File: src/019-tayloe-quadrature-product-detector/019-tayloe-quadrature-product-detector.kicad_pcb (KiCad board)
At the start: 2 copper layers, 20 x 65 mm, 30 parts, among them J1 CONN, J2 CONN, J3 CONN, J4 CONN, J5 CONN, J6 CONN, J7 VCC, J8 VA, J9 VE, U1 74LVX74MTCX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

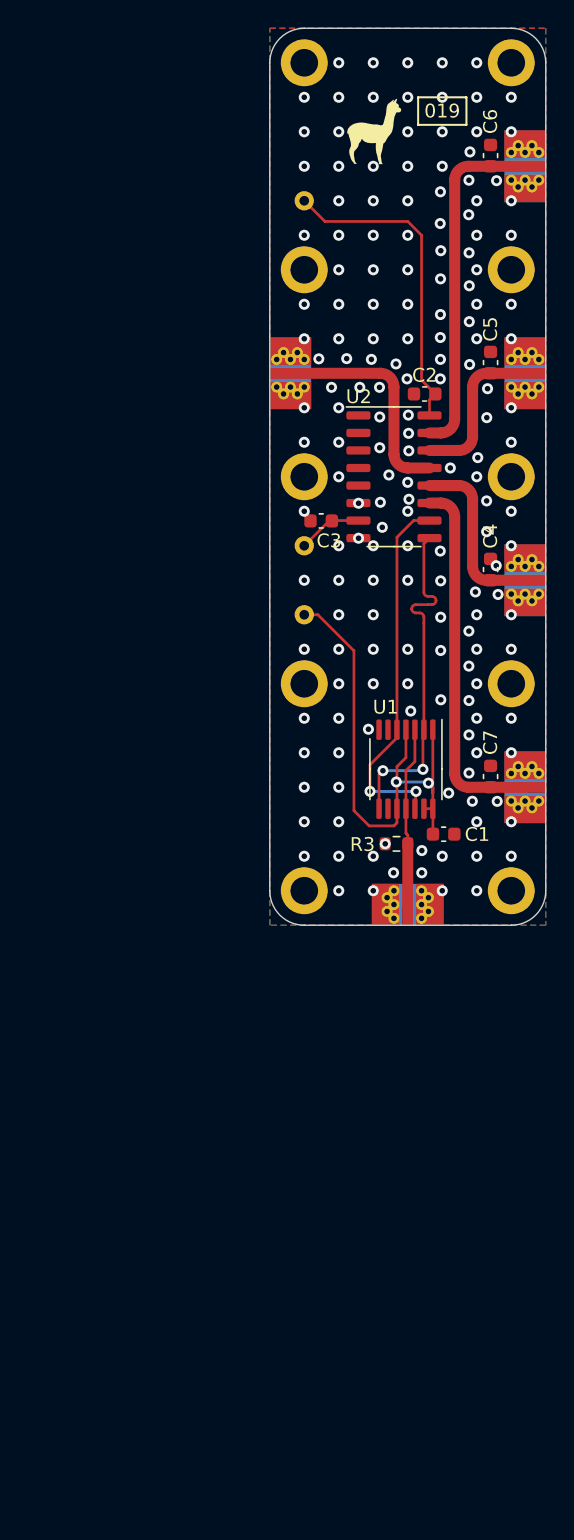
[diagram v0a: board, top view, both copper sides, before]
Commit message: Updating 019-tayloe-quadrature-product-detector for widing port spacing
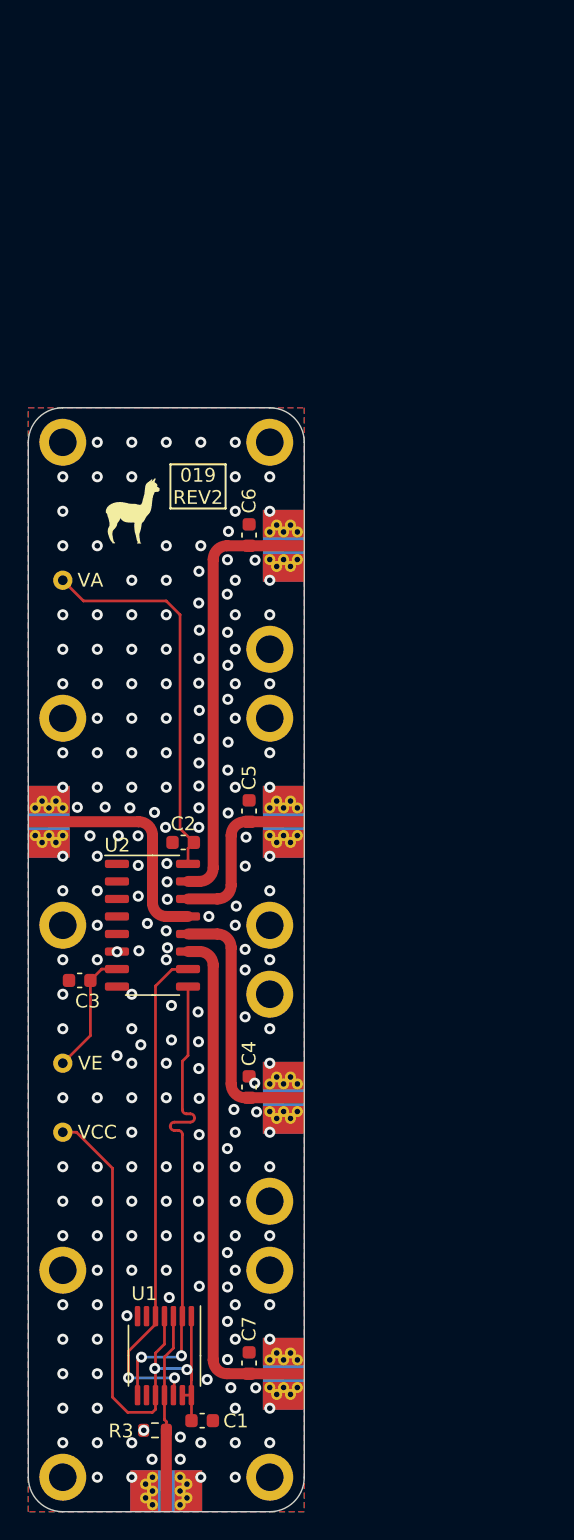
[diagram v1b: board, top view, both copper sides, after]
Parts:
- added H11: M2, modular-rf-bench-footprints:M2-hole, F.Cu at (150.0, 80.0)
- added H12: M2, modular-rf-bench-footprints:M2-hole, F.Cu at (150.0, 115.0)
- added H13: M2, modular-rf-bench-footprints:M2-hole, F.Cu at (150.0, 100.0)
- moved C1 46.0 mm to (145.1, 130.9)
- moved C7 46.0 mm to (148.5, 126.7)
- moved H1 46.0 mm to (135.0, 120.0)
- moved H2 46.0 mm to (135.0, 135.0)
- moved H3 46.0 mm to (150.0, 135.0)
- moved H4 46.0 mm to (150.0, 120.0)
- moved J1 46.0 mm to (142.5, 137.5)
- moved J2 46.0 mm to (152.5, 127.5)
- moved R3 46.0 mm to (141.7, 131.6)
- moved U1 46.0 mm to (142.4, 126.2)
- moved C4 41.4 mm to (148.5, 106.7)
- moved J3 41.4 mm to (152.5, 107.5)
- moved J7 41.4 mm to (135.0, 110.0)
- moved J9 41.4 mm to (135.0, 105.0)
- moved C3 37.6 mm to (136.2, 99.0)
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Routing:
- net /CLK2: track 25.4 -> 35.4 mm
- net /0: track 26.6 -> 36.6 mm
- net /CLK1: track 26.7 -> 36.7 mm
- net /VA: track 23.2 -> 28.2 mm
- net /180: track 12.9 -> 17.9 mm
- net /90: track 25.3 -> 30.3 mm
- net /VE: track 4.68 -> 9.10 mm
- net /VCC: track 39.8 -> 43.6 mm
- net GND: vias 172 -> 201
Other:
- board size 20 x 65 mm -> 20 x 80 mm
- board text added: "019 REV2"
- board text removed: "019"
